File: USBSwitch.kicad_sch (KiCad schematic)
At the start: 5 parts, among them J1 USB_B_Micro, J2 USB_B_Micro, J3 Conn_01x02_Pin

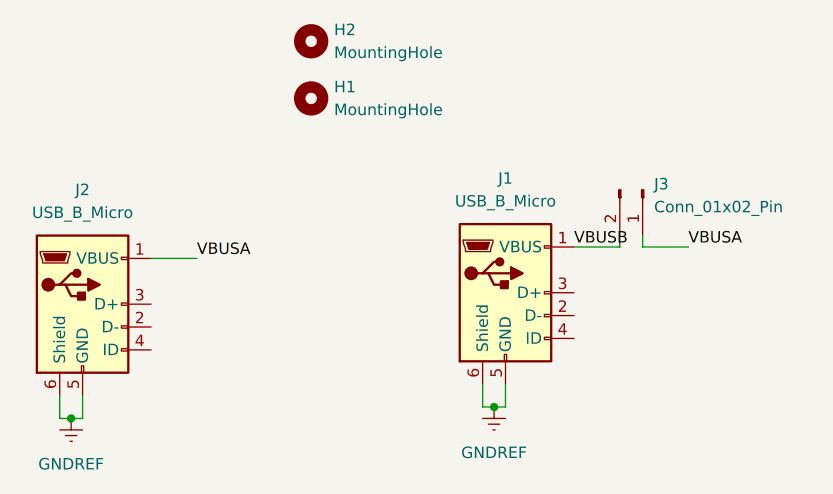
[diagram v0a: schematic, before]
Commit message: Replace one micro-USB with USB-A
It's surprisingly hard to find micro-USB to micro-USB cables that can
handle full USB 2.0 current, so replace one of the connectors with a
USB-A since USB-A to micro-USB cables are plentiful
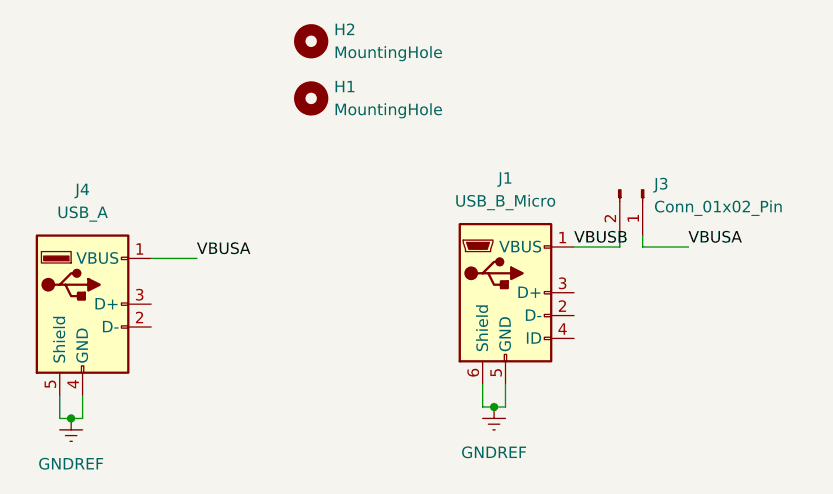
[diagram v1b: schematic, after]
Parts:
- removed J2: USB_B_Micro, Connector_USB:USB_Micro-B_Wuerth_629105150521, symbol Connector:USB_B_Micro
- added J4: USB_A, Connector_USB:USB_A_Molex_67643_Horizontal, symbol Connector:USB_A
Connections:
- net GNDREF: now also J4.4 (GND), J4.5 (Shield)
- net VBUSA: now also J4.1 (VBUS)
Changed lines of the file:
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@@
 	)
 	(symbol
-		(lib_id "Connector:USB_B_Micro")
+		(lib_id "Connector:USB_A")
 		(at 50.8 58.42 0)
 		(unit 1)
@@
 		(dnp no)
 		(fields_autoplaced yes)
-		(property "Reference" "J2"
+		(property "Reference" "J4"
 			(at 50.8 45.72 0)
 			(effects
@@
 			)
 		)
-		(property "Value" "USB_B_Micro"
+		(property "Value" "USB_A"
 			(at 50.8 48.26 0)
 			(effects
@@
 			)
 		)
-		(property "Footprint" "Connector_USB:USB_Micro-B_Wuerth_629105150521"
+		(property "Footprint" "Connector_USB:USB_A_Molex_67643_Horizontal"
 			(at 54.61 59.69 0)
 			(effects
@@
 			)
 		)
-		(property "Description" "USB Micro Type B connector"
+		(property "Description" "USB Type A connector"
 			(at 50.8 58.42 0)
 			(effects
@@
 		(pin "5"
 		)
+		(pin "4"
+		)
 		(pin "2"
-		)
-		(pin "6"
-		)
-		(pin "4"
 		)
 		(pin "3"
 		)
 		(instances
-			(project "USBSwitch"
+			(project ""
 				(path "/1a2285c3-e3ec-4f8a-8fa4-77e392b6d97e"
-					(reference "J2")
+					(reference "J4")
 					(unit 1)
 				)
